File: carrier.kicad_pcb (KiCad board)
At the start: 2 copper layers, 30 x 48 mm, 28 parts, among them J1 Conn_02x06_Odd_Even, J2 DB15_Female_HighDensity, J3 USB_B_Micro, SW1 SW_Push_hrs, SW2 SW_Push_min, SW3 SW_Push_sec, U1 CARAVEL, U2 W25Q32JVSSIQ-TR, U5 MCP1824T-1802E/OT, U6 MIC5504-3.3YM5-TR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

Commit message: updated board with OSHW mark
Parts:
- moved G*** 1.08 mm to (42.7, 69.5)

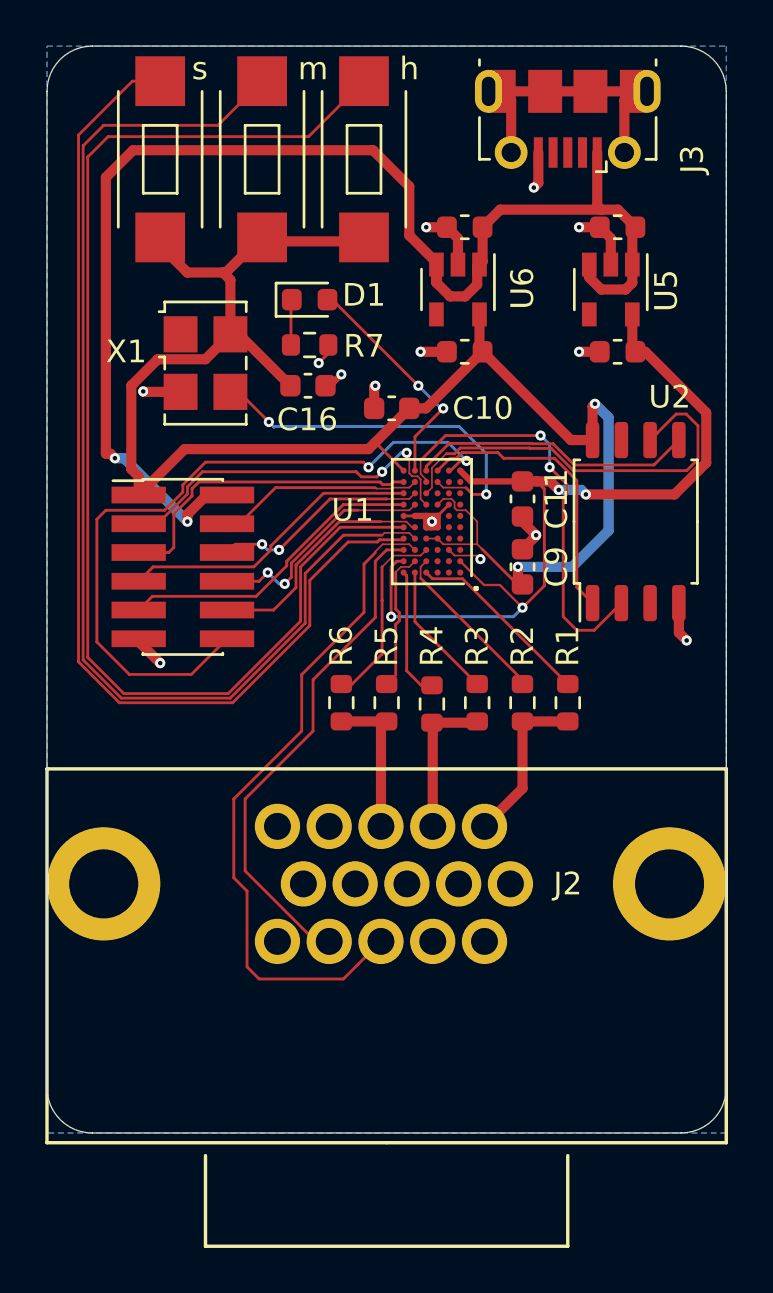
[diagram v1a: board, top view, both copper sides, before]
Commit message: switch to 3.2x2.5 9mhz oscillator, only use 3/3 right under ASIC
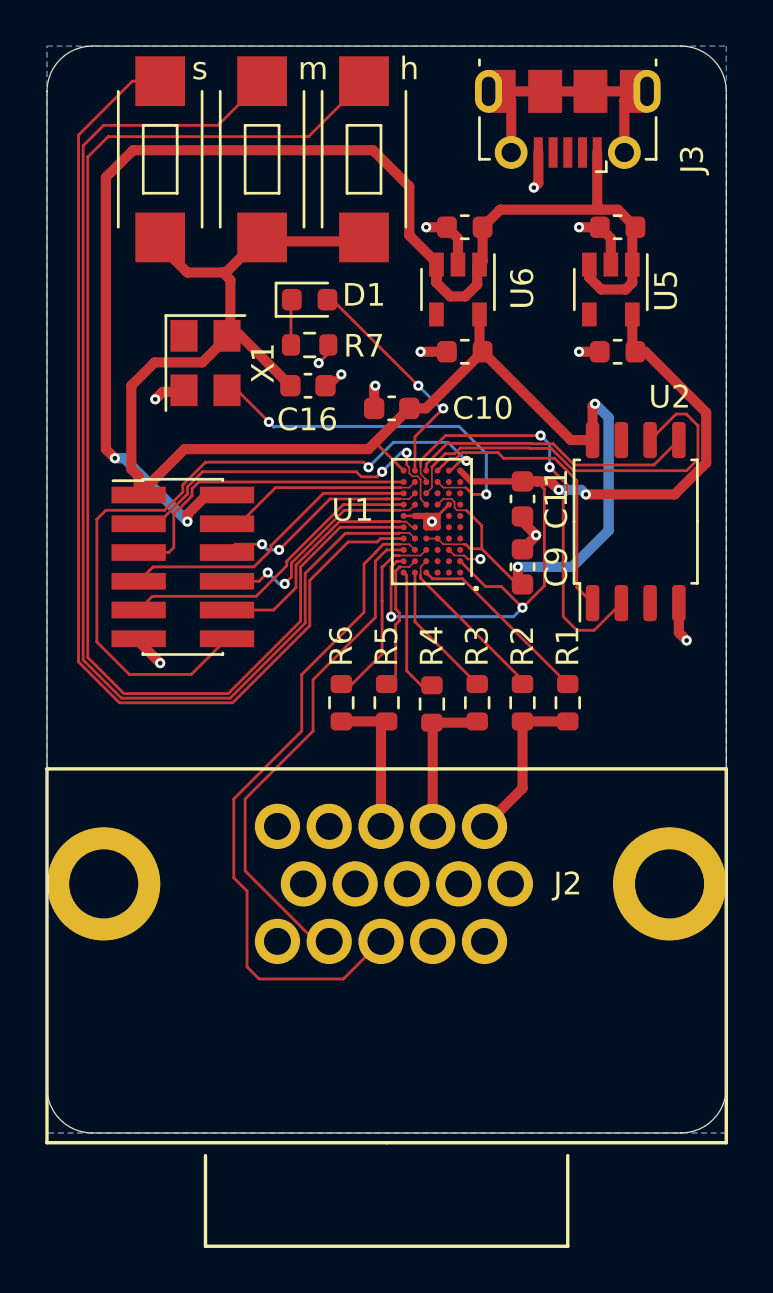
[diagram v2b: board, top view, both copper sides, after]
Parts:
- removed G***: LOGO, carrier:oshw-logo-small
- X1: footprint Oscillator:Oscillator_SMD_SeikoEpson_SG8002LB-4Pin_5.0x3.2mm -> Oscillator:Oscillator_SMD_SeikoEpson_SG8002CE-4Pin_3.2x2.5mm
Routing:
- net mprj_io[7]: track 10.6 -> 11.5 mm

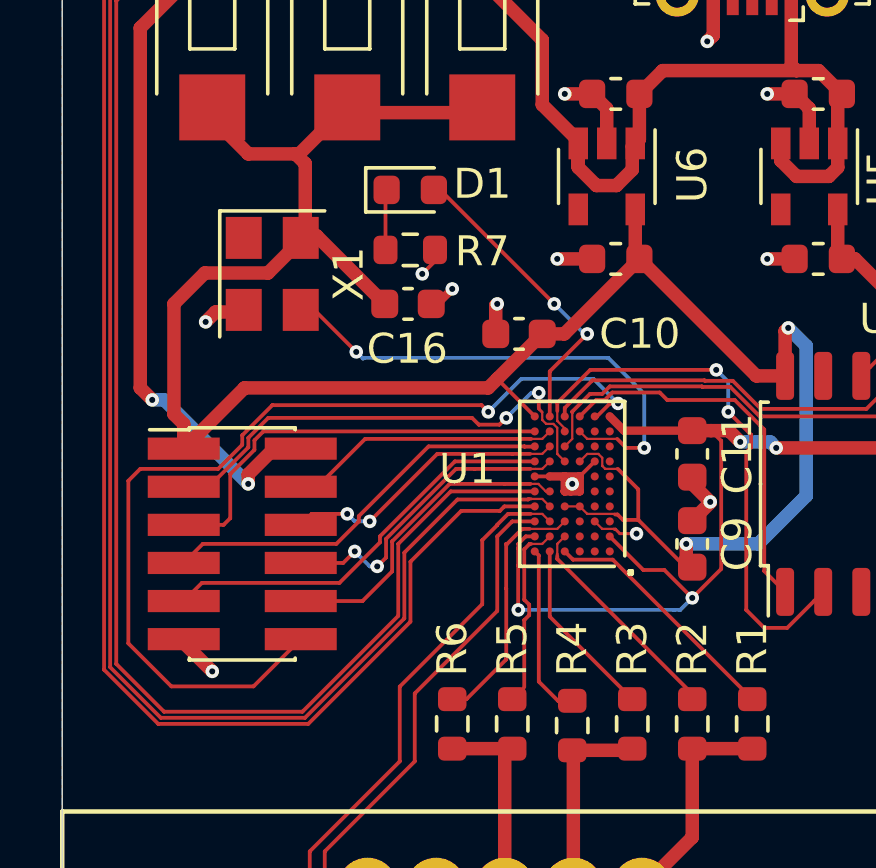
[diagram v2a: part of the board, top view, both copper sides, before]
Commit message: changed programming header to 2x3
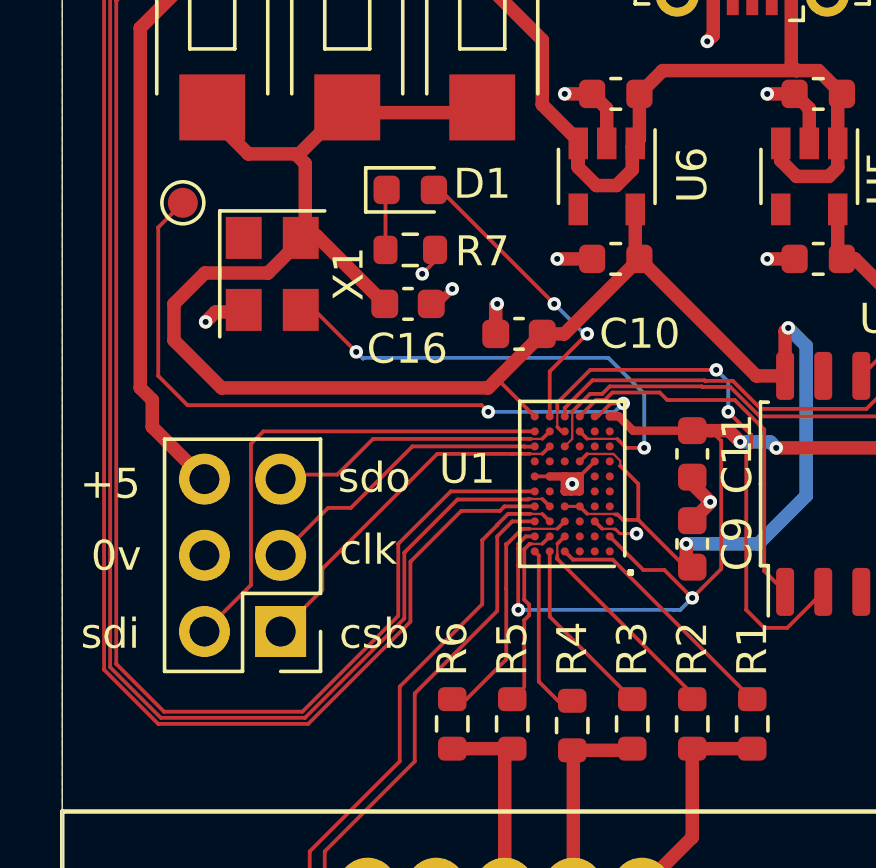
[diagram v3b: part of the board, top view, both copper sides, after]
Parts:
- added G***: LOGO, carrier:oshw-logo-small, B.Cu at (42.7, 67.0)
- added TP1: TestPoint, TestPoint:TestPoint_Pad_D1.0mm, F.Cu at (38.8, 71.6)
- J1: value Conn_02x06_Odd_Even -> Conn_02x03_Counter_Clockwise; footprint Connector_PinHeader_1.27mm:PinHeader_2x06_P1.27mm_Vertical_SMD -> Connector_PinHeader_2.54mm:PinHeader_2x03_P2.54mm_Vertical
- moved J1 3.19 mm to (42.0, 85.9), turned to 180 degrees
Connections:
- J1 pad 1: vdda -> mprj_io[3]
- J1 pad 2: +5V -> mprj_io[2]
- J1 pad 3: mprj_io[0] -> mprj_io[4]
- J1 pad 4: mprj_io[1] -> GND
- J1 pad 5: mprj_io[2] -> mprj_io[1]
- J1 pad 6: mprj_io[3] -> +5V
- U1 pad D7: mprj_io[0] -> Net-(U1-PadD7)
- U1 pad E5: mprj_io[7] -> Net-(U1-PadE5)
- U1 pad E7: mprj_io[5] -> Net-(U1-PadE7)
- U1 pad F7: mprj_io[6] -> Net-(U1-PadF7)
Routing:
- net mprj_io[0]: track 16.5 -> 0.00 mm, vias 2 -> 0
- net mprj_io[6]: track 13.7 -> 0.00 mm
- net mprj_io[7]: track 11.5 -> 0.00 mm
- net mprj_io[5]: track 10.5 -> 0.00 mm, vias 2 -> 0
- net resetb: track 32.8 -> 23.4 mm
- net vdda: track 76.3 -> 72.8 mm
- net mprj_io[4]: track 13.4 -> 9.98 mm
- net +5V: track 59.7 -> 56.2 mm, vias 2 -> 0
- net mprj_io[2]: track 14.0 -> 16.5 mm
- net mprj_io[3]: track 9.59 -> 11.9 mm, vias 2 -> 0
- net GND: track 25.2 -> 23.7 mm, vias 14 -> 13
- net mprj_io[1]: track 9.14 -> 9.71 mm
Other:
- board text added: "+5"
- board text added: "0v"
- board text added: "clk"
- board text added: "csb"
- board text added: "sdi"
- board text added: "sdo"

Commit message: test points, added managment area psu notes to readme
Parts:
- removed G***: LOGO, carrier:oshw-logo-small
- added TP10: TestPoint, TestPoint:TestPoint_Pad_D1.0mm, F.Cu at (63.0, 69.0)
- added TP11: TestPoint, TestPoint:TestPoint_Pad_D1.0mm, F.Cu at (55.9, 72.6)
- added TP2: TestPoint, TestPoint:TestPoint_Pad_D1.0mm, B.Cu at (60.5, 80.5)
- added TP3: TestPoint, TestPoint:TestPoint_Pad_D1.0mm, B.Cu at (60.5, 82.5)
- added TP4: TestPoint, TestPoint:TestPoint_Pad_D1.0mm, B.Cu at (62.5, 80.5)
- added TP5: TestPoint, TestPoint:TestPoint_Pad_D1.0mm, B.Cu at (62.5, 82.5)
- added TP6: TestPoint, TestPoint:TestPoint_Pad_D1.0mm, B.Cu at (42.6, 76.0)
- added TP7: TestPoint, TestPoint:TestPoint_Pad_D1.0mm, B.Cu at (48.8, 103.2)
- added TP8: TestPoint, TestPoint:TestPoint_Pad_D1.0mm, B.Cu at (46.5, 103.2)
- added TP9: TestPoint, TestPoint:TestPoint_Pad_D1.0mm, F.Cu at (63.0, 72.5)
- renumbered U1 to ASIC1
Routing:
- net mprj_io[12]: track 22.5 -> 26.5 mm
- net mprj_io[11]: track 30.0 -> 33.9 mm
- net flash_io1: track 18.7 -> 22.1 mm, vias 2 -> 3
- net flash_csb: track 12.7 -> 16.0 mm, vias 0 -> 1
- net flash_io0: track 12.7 -> 15.5 mm, vias 0 -> 1
- net vccd: track 38.6 -> 41.3 mm
- net +5V: track 56.2 -> 58.9 mm
- net flash_clk: track 18.3 -> 20.7 mm, vias 0 -> 1
- net clock: track 16.6 -> 18.8 mm
- net vdda: track 72.8 -> 74.9 mm
- net resetb: track 23.4 -> 22.8 mm

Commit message: missing oshwa logo
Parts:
- added G***: LOGO, carrier:oshw-logo-small, B.Cu at (42.7, 66.9)

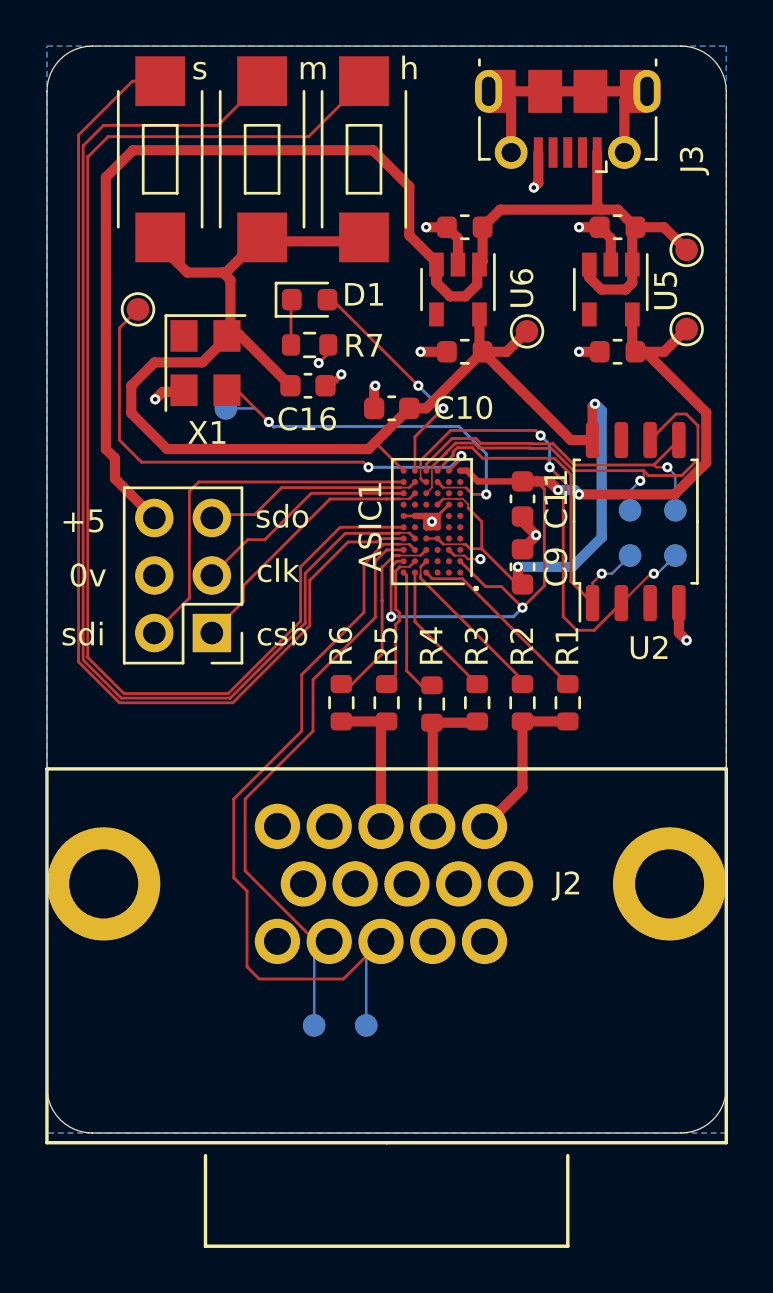
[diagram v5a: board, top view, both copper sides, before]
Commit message: updated to correct asic fp
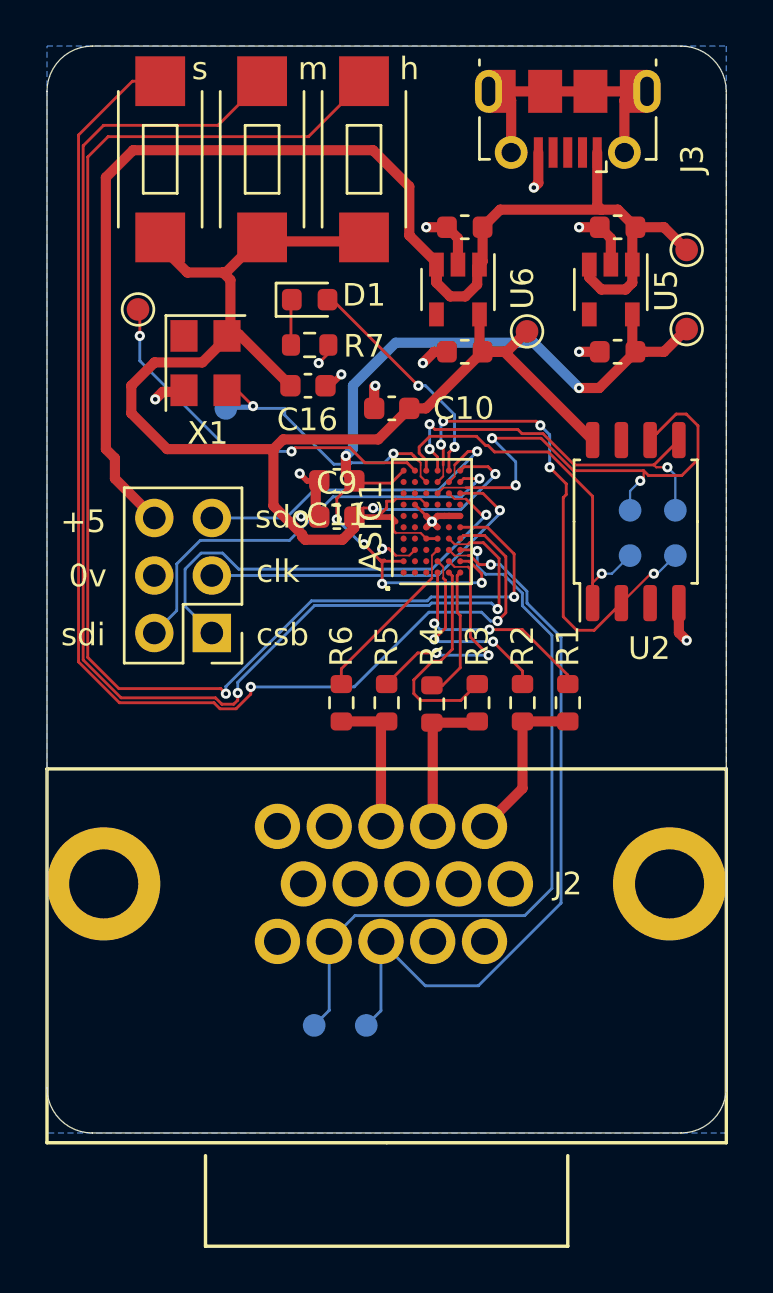
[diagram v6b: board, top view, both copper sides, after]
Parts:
- moved C9 8.49 mm to (47.5, 80.8), turned to 180 degrees
- moved C11 8.24 mm to (47.5, 79.2), turned to 180 degrees
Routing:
- net mprj_io[3]: track 11.9 -> 20.2 mm, vias 0 -> 1
- net mprj_io[10]: track 47.1 -> 54.8 mm, vias 0 -> 2
- net mprj_io[8]: track 54.7 -> 61.9 mm, vias 0 -> 2
- net mprj_io[9]: track 51.6 -> 58.2 mm, vias 0 -> 2
- net resetb: track 22.8 -> 16.6 mm
- net mprj_io[4]: track 9.98 -> 16.1 mm, vias 0 -> 1
- net mprj_io[12]: track 26.5 -> 32.3 mm, vias 0 -> 1
- net mprj_io[1]: track 9.71 -> 15.0 mm, vias 0 -> 1
- net clock: track 18.8 -> 13.8 mm
- net mprj_io[14]: track 6.33 -> 10.3 mm, vias 0 -> 2
- net mprj_io[16]: track 6.06 -> 9.55 mm
- net mprj_io[2]: track 16.5 -> 19.3 mm, vias 0 -> 1
- net flash_csb: track 16.0 -> 17.9 mm
- net flash_clk: track 20.7 -> 22.5 mm, vias 1 -> 3
- net vccd: track 41.3 -> 39.5 mm, vias 4 -> 6
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
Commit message: fix flipped asic fp, updated to v0.2, added ground testpad, added silk version, notes on testing the regs and clock
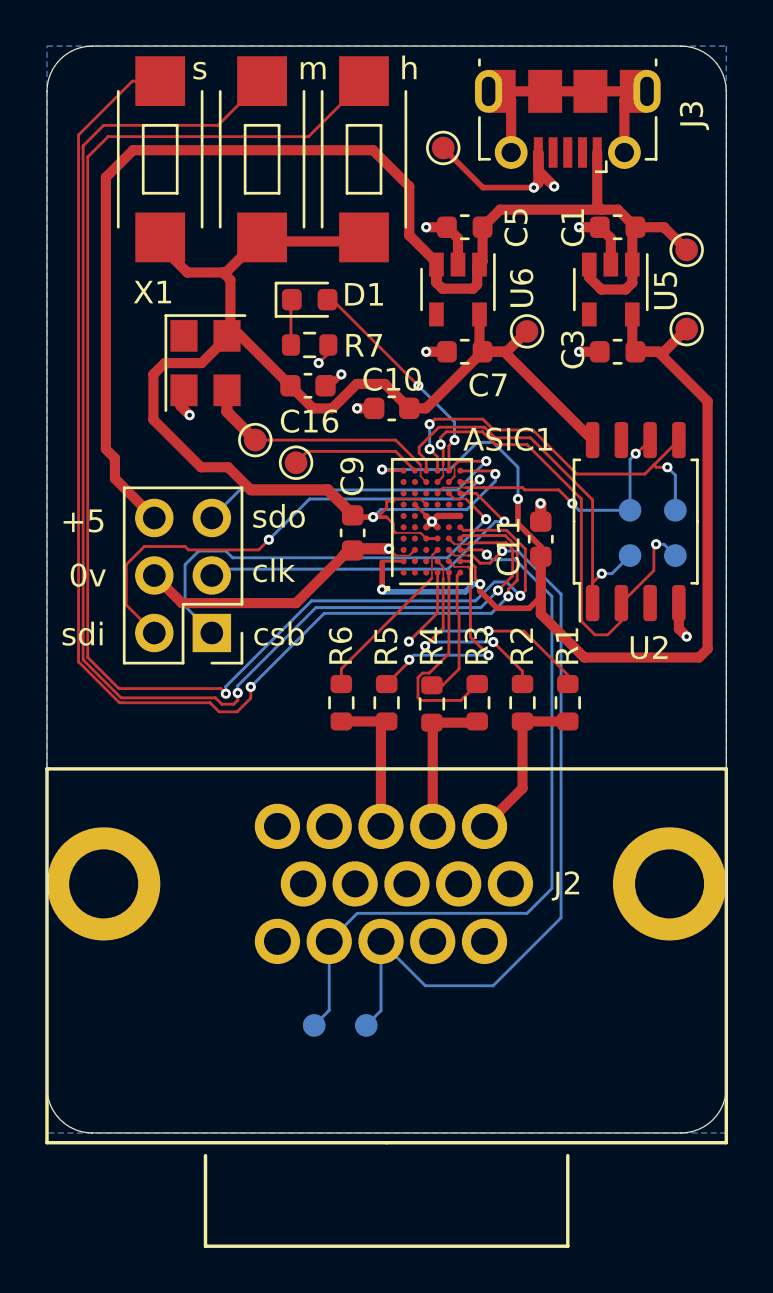
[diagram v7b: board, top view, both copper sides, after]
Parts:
- added TP12: TestPoint, TestPoint:TestPoint_Pad_D1.0mm, F.Cu at (52.2, 64.5)
- TP6: moved to F.Cu
- moved TP1 9.72 mm to (45.7, 78.4)
- moved C11 9.37 mm to (56.5, 81.8), turned to 90 degrees
- moved TP6 1.91 mm to (43.9, 77.4)
- moved C9 0.99 mm to (48.2, 81.5), turned to 270 degrees
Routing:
- net vccd: track 39.5 -> 56.6 mm, vias 6 -> 4
- net GND: track 23.9 -> 38.4 mm
- net resetb: track 16.6 -> 5.81 mm, vias 2 -> 0
- net flash_clk: track 22.5 -> 12.5 mm, vias 3 -> 2
- net vdda: track 75.5 -> 70.1 mm
- net clock: track 13.8 -> 11.3 mm, vias 2 -> 0
- net mprj_io[2]: track 19.3 -> 21.7 mm, vias 1 -> 2
- net mprj_io[18]: track 9.55 -> 12.0 mm
- net mprj_io[11]: track 32.9 -> 34.5 mm
- net mprj_io[8]: track 61.9 -> 63.4 mm
- net mprj_io[17]: track 8.86 -> 9.66 mm
- net flash_io0: track 17.1 -> 17.6 mm
- net flash_io1: track 22.8 -> 22.4 mm, vias 5 -> 2
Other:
- board text added: "version 0.2"
